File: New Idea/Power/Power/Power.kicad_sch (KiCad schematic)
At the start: 3 parts, among them J1 Conn_PinHeader_1x02_P2.54mm_H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, J2 Conn_PinHeader_1x04_P2.54mm_H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, U1 Regulator_Linear_NCP1117-5.0V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

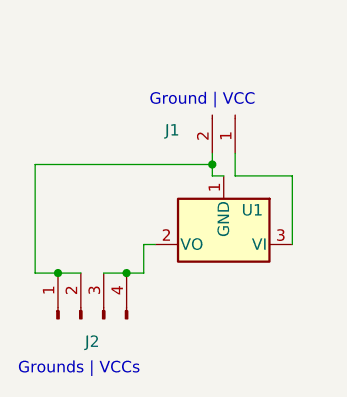
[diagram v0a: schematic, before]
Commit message: v3.5 - Code Updates, Mill File, 3D Models
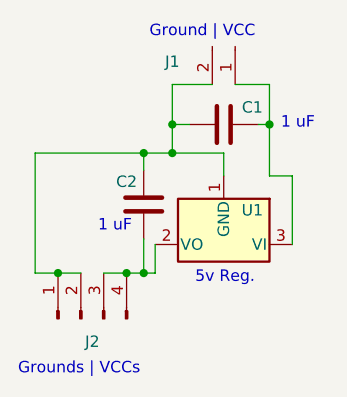
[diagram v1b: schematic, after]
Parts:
- added C1, C2: C, fab:C_1206, symbol Fab Library:C
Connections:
- net at J1.1, U1.3 (VI): now also C1.2
- net at J1.2, J2.1 (Pin_1), J2.2 (Pin_2)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: now also C1.1, C2.2
- net at J2.3 (Pin_3), J2.4 (Pin_4), U1.2 (VO): now also C2.1
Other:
- note added: "1 uF"
- note added: "5v Reg."
- moved on the sheet: J1
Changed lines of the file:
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@@
   (junction (at 118.11 73.66) (diameter 0) (color 0 0 0 0)
   )
-  (junction (at 135.255 61.595) (diameter 0) (color 0 0 0 0)
+  (junction (at 141.605 57.15) (diameter 0) (color 0 0 0 0)
+  )
+  (junction (at 130.81 60.325) (diameter 0) (color 0 0 0 0)
+  )
+  (junction (at 130.81 57.15) (diameter 0) (color 0 0 0 0)
+  )
+  (junction (at 127.635 60.325) (diameter 0) (color 0 0 0 0)
+  )
+  (junction (at 127.635 73.66) (diameter 0) (color 0 0 0 0)
   )
   (junction (at 125.73 73.66) (diameter 0) (color 0 0 0 0)
   )
-  (wire (pts (xy 135.255 60.325) (xy 135.255 61.595))
+  (wire (pts (xy 130.81 52.705) (xy 130.81 57.15))
     (stroke (width 0) (type default) (color 0 0 0 0))
   )
-  (wire (pts (xy 135.255 62.865) (xy 136.525 62.865))
+  (wire (pts (xy 141.605 57.15) (xy 141.605 52.705))
     (stroke (width 0) (type default) (color 0 0 0 0))
   )
-  (wire (pts (xy 135.255 61.595) (xy 135.255 62.865))
+  (wire (pts (xy 130.81 57.15) (xy 132.715 57.15))
+    (stroke (width 0) (type default) (color 0 0 0 0))
+  )
+  (wire (pts (xy 136.525 60.325) (xy 136.525 62.865))
     (stroke (width 0) (type default) (color 0 0 0 0))
   )
@@
     (stroke (width 0) (type default) (color 0 0 0 0))
   )
-  (wire (pts (xy 128.905 70.485) (xy 127.635 70.485))
+  (wire (pts (xy 128.905 73.66) (xy 127.635 73.66))
     (stroke (width 0) (type default) (color 0 0 0 0))
   )
-  (wire (pts (xy 144.145 62.865) (xy 137.795 62.865))
+  (wire (pts (xy 144.145 62.865) (xy 141.605 62.865))
+    (stroke (width 0) (type default) (color 0 0 0 0))
+  )
+  (wire (pts (xy 127.635 60.325) (xy 127.635 62.23))
+    (stroke (width 0) (type default) (color 0 0 0 0))
+  )
+  (wire (pts (xy 130.81 57.15) (xy 130.81 60.325))
     (stroke (width 0) (type default) (color 0 0 0 0))
   )
@@
     (stroke (width 0) (type default) (color 0 0 0 0))
   )
+  (wire (pts (xy 140.335 57.15) (xy 141.605 57.15))
+    (stroke (width 0) (type default) (color 0 0 0 0))
+  )
   (wire (pts (xy 118.11 73.66) (xy 120.65 73.66))
     (stroke (width 0) (type default) (color 0 0 0 0))
   )
-  (wire (pts (xy 115.57 61.595) (xy 135.255 61.595))
+  (wire (pts (xy 128.905 73.66) (xy 128.905 70.485))
     (stroke (width 0) (type default) (color 0 0 0 0))
   )
-  (wire (pts (xy 137.795 62.865) (xy 137.795 60.325))
+  (wire (pts (xy 115.57 60.325) (xy 127.635 60.325))
+    (stroke (width 0) (type default) (color 0 0 0 0))
+  )
+  (wire (pts (xy 141.605 52.705) (xy 137.795 52.705))
+    (stroke (width 0) (type default) (color 0 0 0 0))
+  )
+  (wire (pts (xy 141.605 62.865) (xy 141.605 57.15))
+    (stroke (width 0) (type default) (color 0 0 0 0))
+  )
+  (wire (pts (xy 130.81 52.705) (xy 135.255 52.705))
     (stroke (width 0) (type default) (color 0 0 0 0))
   )
@@
     (stroke (width 0) (type default) (color 0 0 0 0))
   )
-  (wire (pts (xy 127.635 70.485) (xy 127.635 73.66))
+  (wire (pts (xy 127.635 60.325) (xy 130.81 60.325))
     (stroke (width 0) (type default) (color 0 0 0 0))
   )
-  (wire (pts (xy 115.57 61.595) (xy 115.57 73.66))
+  (wire (pts (xy 127.635 69.85) (xy 127.635 73.66))
+    (stroke (width 0) (type default) (color 0 0 0 0))
+  )
+  (wire (pts (xy 115.57 60.325) (xy 115.57 73.66))
+    (stroke (width 0) (type default) (color 0 0 0 0))
+  )
+  (wire (pts (xy 130.81 60.325) (xy 136.525 60.325))
     (stroke (width 0) (type default) (color 0 0 0 0))
   )
@@
     (effects (font (size 1.27 1.27)) (justify left bottom))
   )
-  (text "Ground | VCC" (at 128.27 55.245 0)
+  (text "1 uF" (at 122.555 69.215 0)
     (effects (font (size 1.27 1.27)) (justify left bottom))
   )
-  (symbol (lib_id "Fab Library:Conn_PinHeader_1x02_P2.54mm_Horizontal_SMD") (at 137.795 55.245 270) (unit 1)
+  (text "Ground | VCC" (at 128.27 47.625 0)
+    (effects (font (size 1.27 1.27)) (justify left bottom))
+  )
+  (text "5v Reg." (at 133.35 74.93 0)
+    (effects (font (size 1.27 1.27)) (justify left bottom))
+  )
+  (text "1 uF" (at 142.875 57.785 0)
+    (effects (font (size 1.27 1.27)) (justify left bottom))
+  )
+  (symbol (lib_id "Fab Library:Conn_PinHeader_1x02_P2.54mm_Horizontal_SMD") (at 137.795 47.625 270) (unit 1)
     (in_bom yes) (on_board yes)
-    (property "Reference" "J1" (id 0) (at 130.81 57.785 90))
-    (property "Value" "Conn_PinHeader_1x02_P2.54mm_Horizontal_SMD" (id 1) (at 136.525 53.975 90)
+    (property "Reference" "J1" (id 0) (at 130.81 50.165 90))
+    (property "Value" "Conn_PinHeader_1x02_P2.54mm_Horizontal_SMD" (id 1) (at 136.525 46.355 90)
       (effects (font (size 1.27 1.27)) hide)
     )
-    (property "Footprint" "fab:PinHeader_UPDI_01x02_P2.54mm_Horizontal_SMD" (id 2) (at 137.795 55.245 0)
+    (property "Footprint" "fab:PinHeader_UPDI_01x02_P2.54mm_Horizontal_SMD" (id 2) (at 137.795 47.625 0)
       (effects (font (size 1.27 1.27)) hide)
     )
-    (property "Datasheet" "~" (id 3) (at 137.795 55.245 0)
+    (property "Datasheet" "~" (id 3) (at 137.795 47.625 0)
+      (effects (font (size 1.27 1.27)) hide)
+    )
+    (pin "1")
+    (pin "2")
+  )
+  (symbol (lib_id "Fab Library:C") (at 136.525 57.15 90) (unit 1)
+    (in_bom yes) (on_board yes)
+    (property "Reference" "C1" (id 0) (at 139.7 55.245 90))
+    (property "Value" "C" (id 1) (at 136.525 52.07 90)
+      (effects (font (size 1.27 1.27)) hide)
+    )
+    (property "Footprint" "fab:C_1206" (id 2) (at 140.335 56.1848 0)
+      (effects (font (size 1.27 1.27)) hide)
+    )
+    (property "Datasheet" "" (id 3) (at 136.525 57.15 0)
       (effects (font (size 1.27 1.27)) hide)
     )
@@
     (pin "4")
   )
+  (symbol (lib_id "Fab Library:C") (at 127.635 66.04 180) (unit 1)
+    (in_bom yes) (on_board yes)
+    (property "Reference" "C2" (id 0) (at 125.73 63.5 0))
+    (property "Value" "C" (id 1) (at 122.555 66.04 90)
+      (effects (font (size 1.27 1.27)) hide)
+    )
+    (property "Footprint" "fab:C_1206" (id 2) (at 126.6698 62.23 0)
+      (effects (font (size 1.27 1.27)) hide)
+    )
+    (property "Datasheet" "" (id 3) (at 127.635 66.04 0)
+      (effects (font (size 1.27 1.27)) hide)
+    )
+    (pin "1")
+    (pin "2")
+  )
   (symbol (lib_id "Fab Library:Regulator_Linear_NCP1117-5.0V-1A") (at 136.525 70.485 180) (unit 1)
     (in_bom yes) (on_board yes)
@@
   )
   (symbol_instances
+    (path "/6540157e-dd56-419f-8e12-b9f763e7e5a8"
+      (reference "C1") (unit 1) (value "C") (footprint "fab:C_1206")
+    )
+    (path "/7c8c6616-3f53-450b-af3f-09c3faf9c953"
+      (reference "C2") (unit 1) (value "C") (footprint "fab:C_1206")
+    )
     (path "/32ffa73f-a777-4724-b8ef-1ba30c979ef3"
       (reference "J1") (unit 1) (value "Conn_PinHeader_1x02_P2.54mm_Horizontal_SMD") (footprint "fab:PinHeader_UPDI_01x02_P2.54mm_Horizontal_SMD")
